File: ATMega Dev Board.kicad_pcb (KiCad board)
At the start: 4 copper layers, 84 x 38.1 mm, 50 parts, among them J1 Conn_01x13, J2 Conn_01x09, J4 SPI header, J5 USB-C_31-M-12, Q1 S8050, Q2 2N7002, Q3 HL6042, Q4 HL6042, SW1 SW_SPST, SW2 SW_SPST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

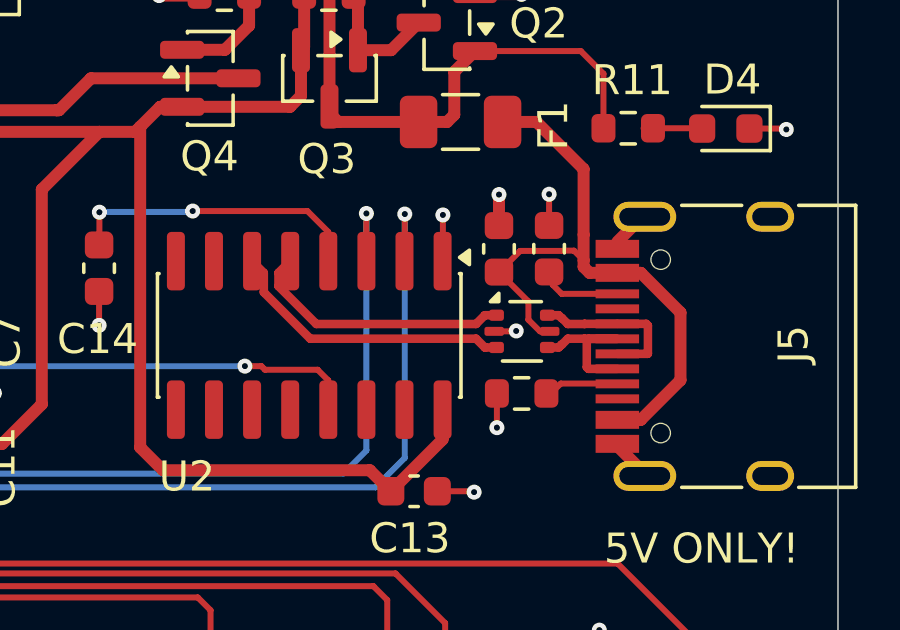
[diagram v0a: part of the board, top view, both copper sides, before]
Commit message: new stackup
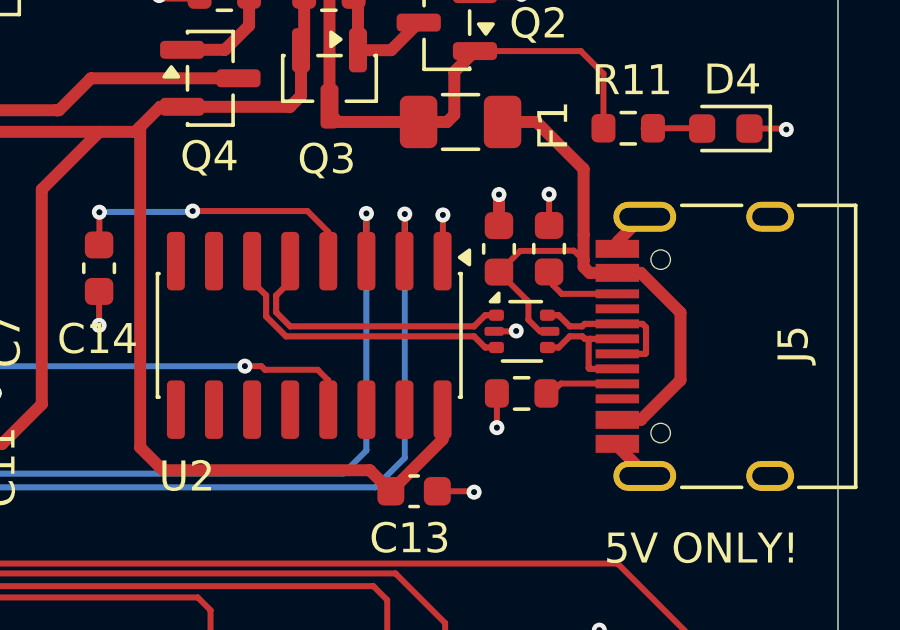
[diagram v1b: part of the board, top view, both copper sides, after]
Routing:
- net /UD_N: track 5.43 -> 4.48 mm
- net /UD+: track 8.90 -> 9.59 mm
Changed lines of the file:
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@@
 	(generator_version "9.0")
 	(general
-		(thickness 1.6062)
+		(thickness 1.586)
 		(legacy_teardrops no)
 	)
@@
 				(type "prepreg")
 				(color "FR4 natural")
-				(thickness 0.2104)
+				(thickness 0.203)
 				(material "FR4")
 				(epsilon_r 4.4)
@@
 			(layer "In1.Cu"
 				(type "copper")
-				(thickness 0.0152)
+				(thickness 0.03)
 			)
 			(layer "dielectric 2"
 				(type "core")
-				(thickness 1.065)
+				(thickness 1.03)
 				(material "FR4")
 				(epsilon_r 4.6)
@@
 			(layer "In2.Cu"
 				(type "copper")
-				(thickness 0.0152)
+				(thickness 0.03)
 			)
 			(layer "dielectric 3"
 				(type "prepreg")
 				(color "FR4 natural")
-				(thickness 0.2104)
+				(thickness 0.203)
 				(material "FR4")
 				(epsilon_r 4.4)
@@
 			)
 			(copper_finish "HAL lead-free")
-			(dielectric_constraints no)
+			(dielectric_constraints yes)
 		)
 		(pad_to_mask_clearance 0)
@@
 	)
 	(segment
-		(start 109.775676 71.5454)
-		(end 110.068576 71.2525)
-		(width 0.286)
+		(start 103.11175 71.15593)
+		(end 103.57907 71.62325)
+		(width 0.2065)
 		(layer "F.Cu")
 		(net 23)
 	)
 	(segment
-		(start 103.1896 69.8404)
-		(end 103.1896 70.283682)
-		(width 0.286)
+		(start 103.57907 71.62325)
+		(end 109.709249 71.62325)
+		(width 0.2065)
 		(layer "F.Cu")
 		(net 23)
 	)
 	(segment
-		(start 103.58 69.45)
-		(end 103.1896 69.8404)
-		(width 0.286)
+		(start 103.58 70.125)
+		(end 103.11175 70.59325)
+		(width 0.2065)
 		(layer "F.Cu")
 		(net 23)
 	)
 	(segment
-		(start 110.068576 71.2525)
+		(start 109.709249 71.62325)
 		(end 110.079999 71.2525)
-		(width 0.286)
+		(width 0.2065)
 		(layer "F.Cu")
 		(net 23)
@@
 		(start 110.079999 71.2525)
 		(end 110.455 71.2525)
-		(width 0.286)
+		(width 0.2065)
 		(layer "F.Cu")
 		(net 23)
 	)
 	(segment
-		(start 103.1896 70.283682)
-		(end 104.451318 71.5454)
-		(width 0.286)
+		(start 103.11175 70.59325)
+		(end 103.11175 71.15593)
+		(width 0.2065)
 		(layer "F.Cu")
 		(net 23)
 	)
 	(segment
-		(start 104.451318 71.5454)
-		(end 109.775676 71.5454)
-		(width 0.286)
+		(start 103.58 69.45)
+		(end 103.58 70.125)
+		(width 0.2065)
 		(layer "F.Cu")
 		(net 23)
 	)
 	(segment
-		(start 110.068576 72.3275)
-		(end 110.079999 72.3275)
-		(width 0.286)
+		(start 102.31 69.45)
+		(end 102.31 70.125)
+		(width 0.2065)
 		(layer "F.Cu")
 		(net 24)
 	)
 	(segment
-		(start 104.248682 72.0346)
-		(end 109.775676 72.0346)
-		(width 0.286)
+		(start 110.079999 72.3275)
+		(end 110.455 72.3275)
+		(width 0.2065)
 		(layer "F.Cu")
 		(net 24)
 	)
 	(segment
-		(start 110.079999 72.3275)
-		(end 110.455 72.3275)
-		(width 0.286)
+		(start 109.709249 71.95675)
+		(end 110.079999 72.3275)
+		(width 0.2065)
 		(layer "F.Cu")
 		(net 24)
 	)
 	(segment
-		(start 102.7004 70.486318)
-		(end 104.248682 72.0346)
-		(width 0.286)
+		(start 103.44093 71.95675)
+		(end 109.709249 71.95675)
+		(width 0.2065)
 		(layer "F.Cu")
 		(net 24)
 	)
 	(segment
-		(start 109.775676 72.0346)
-		(end 110.068576 72.3275)
-		(width 0.286)
+		(start 102.31 70.125)
+		(end 102.77825 70.59325)
+		(width 0.2065)
 		(layer "F.Cu")
 		(net 24)
 	)
 	(segment
-		(start 102.31 69.45)
-		(end 102.7004 69.8404)
-		(width 0.286)
+		(start 102.77825 70.59325)
+		(end 102.77825 71.29407)
+		(width 0.2065)
 		(layer "F.Cu")
 		(net 24)
 	)
 	(segment
-		(start 102.7004 69.8404)
-		(end 102.7004 70.486318)
-		(width 0.286)
+		(start 102.77825 71.29407)
+		(end 103.44093 71.95675)
+		(width 0.2065)
 		(layer "F.Cu")
 		(net 24)
@@
 	)
 	(segment
-		(start 113.466 72.096)
-		(end 113.466 72.984)
-		(width 0.286)
-		(layer "F.Cu")
-		(net 64)
-	)
-	(segment
-		(start 112.155 72.3275)
-		(end 112.530001 72.3275)
-		(width 0.286)
-		(layer "F.Cu")
-		(net 64)
-	)
-	(segment
-		(start 114.485 72.04)
-		(end 113.522 72.04)
-		(width 0.286)
+		(start 112.530001 72.3275)
+		(end 112.900751 71.95675)
+		(width 0.2065)
 		(layer "F.Cu")
 		(net 64)
 	)
 	(segment
-		(start 113.392099 72.0346)
-		(end 113.397499 72.04)
-		(width 0.286)
+		(start 113.397499 72.04)
+		(end 113.58 72.04)
+		(width 0.2065)
 		(layer "F.Cu")
 		(net 64)
 	)
 	(segment
-		(start 113.397499 72.04)
+		(start 113.58 72.04)
 		(end 114.485 72.04)
-		(width 0.286)
+		(width 0.2065)
 		(layer "F.Cu")
 		(net 64)
 	)
 	(segment
-		(start 113.522 72.04)
-		(end 113.466 72.096)
-		(width 0.286)
+		(start 113.58 72.04)
+		(end 113.52875 72.09125)
+		(width 0.2065)
 		(layer "F.Cu")
 		(net 64)
 	)
 	(segment
-		(start 112.634924 72.234)
-		(end 112.834324 72.0346)
-		(width 0.286)
+		(start 113.52875 72.09125)
+		(end 113.52875 73.01525)
+		(width 0.2065)
 		(layer "F.Cu")
 		(net 64)
 	)
 	(segment
-		(start 112.623501 72.234)
-		(end 112.634924 72.234)
-		(width 0.286)
+		(start 113.5535 73.04)
+		(end 114.485 73.04)
+		(width 0.2065)
 		(layer "F.Cu")
 		(net 64)
 	)
 	(segment
-		(start 112.834324 72.0346)
-		(end 113.392099 72.0346)
-		(width 0.286)
+		(start 112.155 72.3275)
+		(end 112.530001 72.3275)
+		(width 0.2065)
 		(layer "F.Cu")
 		(net 64)
 	)
 	(segment
-		(start 113.466 72.984)
-		(end 113.522 73.04)
-		(width 0.286)
+		(start 113.314249 71.95675)
+		(end 113.397499 72.04)
+		(width 0.2065)
 		(layer "F.Cu")
 		(net 64)
 	)
 	(segment
-		(start 113.522 73.04)
-		(end 114.485 73.04)
-		(width 0.286)
+		(start 113.52875 73.01525)
+		(end 113.5535 73.04)
+		(width 0.2065)
 		(layer "F.Cu")
 		(net 64)
 	)
 	(segment
-		(start 112.530001 72.3275)
-		(end 112.623501 72.234)
-		(width 0.286)
+		(start 112.900751 71.95675)
+		(end 113.314249 71.95675)
+		(width 0.2065)
 		(layer "F.Cu")
 		(net 64)
 	)
 	(segment
-		(start 112.155 71.2525)
-		(end 112.530001 71.2525)
-		(width 0.286)
-		(layer "F.Cu")
-		(net 65)
-	)
-	(segment
-		(start 115.448 71.54)
-		(end 115.504 71.596)
-		(width 0.286)
-		(layer "F.Cu")
-		(net 65)
-	)
-	(segment
-		(start 115.496 72.54)
-		(end 114.485 72.54)
-		(width 0.286)
+		(start 112.530001 71.2525)
+		(end 112.900751 71.62325)
+		(width 0.2065)
 		(layer "F.Cu")
 		(net 65)
 	)
 	(segment
-		(start 112.834324 71.5454)
-		(end 113.392099 71.5454)
-		(width 0.286)
+		(start 114.485 71.54)
+		(end 115.3225 71.54)
+		(width 0.2065)
 		(layer "F.Cu")
 		(net 65)
 	)
 	(segment
-		(start 112.530001 71.2525)
-		(end 112.623501 71.346)
-		(width 0.286)
+		(start 115.3225 71.54)
+		(end 115.44125 71.65875)
+		(width 0.2065)
 		(layer "F.Cu")
 		(net 65)
 	)
 	(segment
-		(start 114.485 71.54)
-		(end 115.448 71.54)
-		(width 0.286)
+		(start 113.314249 71.62325)
+		(end 113.397499 71.54)
+		(width 0.2065)
 		(layer "F.Cu")
 		(net 65)
 	)
 	(segment
-		(start 112.623501 71.346)
-		(end 112.634924 71.346)
-		(width 0.286)
+		(start 115.44125 72.51525)
+		(end 115.4165 72.54)
+		(width 0.2065)
 		(layer "F.Cu")
 		(net 65)
 	)
 	(segment
-		(start 113.397499 71.54)
-		(end 114.485 71.54)
-		(width 0.286)
+		(start 115.4165 72.54)
+		(end 114.485 72.54)
+		(width 0.2065)
 		(layer "F.Cu")
 		(net 65)
 	)
 	(segment
-		(start 112.634924 71.346)
-		(end 112.834324 71.5454)
-		(width 0.286)
+		(start 112.155 71.2525)
+		(end 112.530001 71.2525)
+		(width 0.2065)
 		(layer "F.Cu")
 		(net 65)
 	)
 	(segment
-		(start 113.392099 71.5454)
-		(end 113.397499 71.54)
-		(width 0.286)
+		(start 112.900751 71.62325)
+		(end 113.314249 71.62325)
+		(width 0.2065)
 		(layer "F.Cu")
 		(net 65)
 	)
 	(segment
-		(start 115.504 71.596)
-		(end 115.504 72.532)
-		(width 0.286)
+		(start 113.397499 71.54)
+		(end 114.485 71.54)
+		(width 0.2065)
 		(layer "F.Cu")
 		(net 65)
 	)
 	(segment
-		(start 115.504 72.532)
-		(end 115.496 72.54)
-		(width 0.286)
+		(start 115.44125 71.65875)
+		(end 115.44125 72.51525)
+		(width 0.2065)
 		(layer "F.Cu")
 		(net 65)

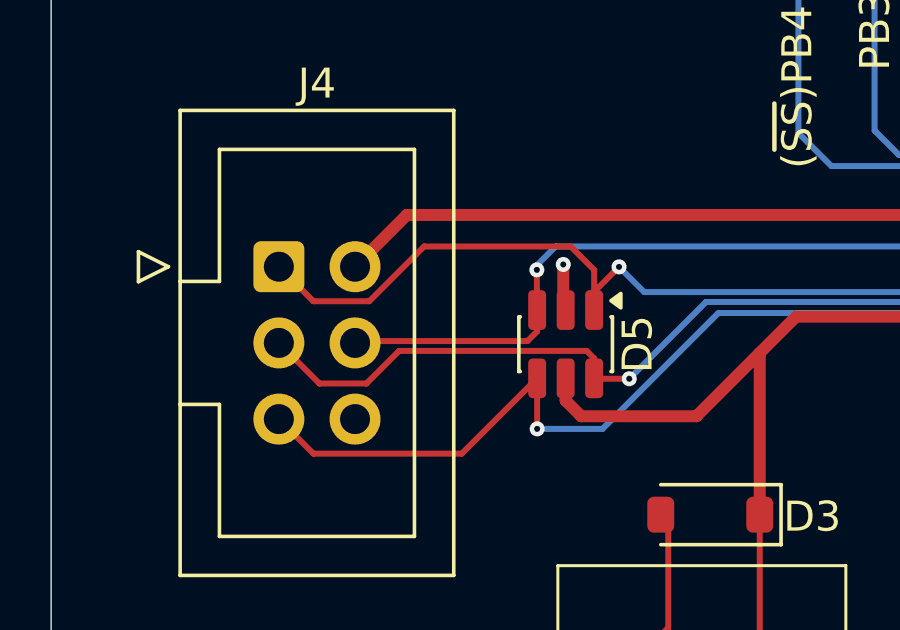
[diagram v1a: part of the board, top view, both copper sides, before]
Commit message: added teardrops
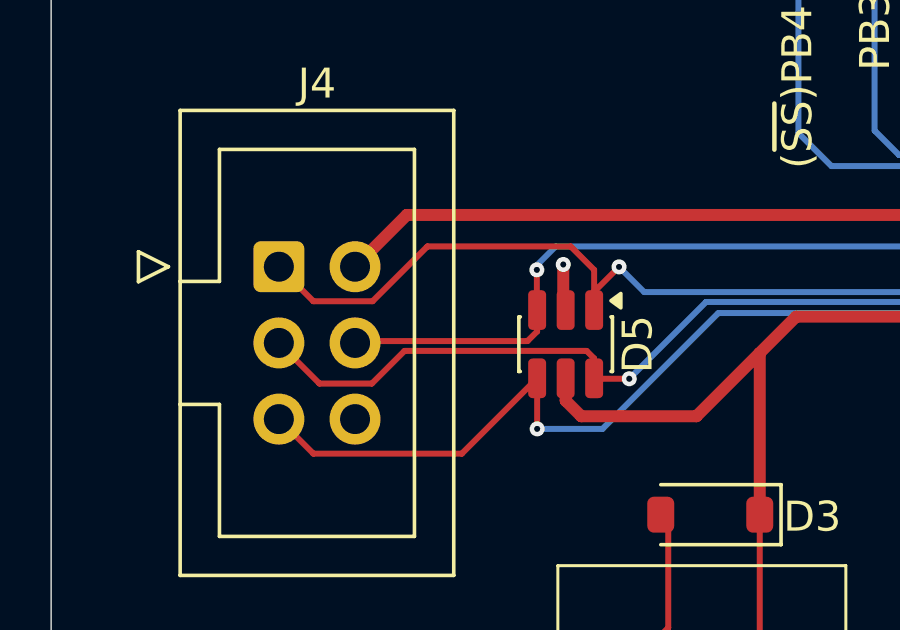
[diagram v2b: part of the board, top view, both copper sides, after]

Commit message: updated constraints and traces
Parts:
- moved C10 0.40 mm to (83.6, 65.8)
- moved C9 0.40 mm to (86.7, 65.8)
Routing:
- net VCC: track 170.3 -> 175.3 mm
- net GND: track 48.0 -> 50.4 mm, vias 33 -> 32
- net VBUS: track 21.5 -> 23.4 mm
- net /RST: track 48.9 -> 48.0 mm
- net /UD_N: track 4.48 -> 5.32 mm
- net /PB0: track 17.8 -> 18.4 mm
